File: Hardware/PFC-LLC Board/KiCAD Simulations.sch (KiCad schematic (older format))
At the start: 31 parts, among them J1 Conn_01x02_Female, P1 Conn_WallPlug_Earth, Q1 C2M0160120D, U1 UCC28180DR

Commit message: Start of PCB
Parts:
- Q1: footprint Package_TO_SOT_THT:TO-247-3_Vertical -> Package_TO_SOT_THT:TO-220-3_Vertical
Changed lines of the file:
@@
 F 0 "Q1" H 8854 2596 50  0000 L CNN
 F 1 "C2M0160120D" H 8854 2505 50  0000 L CNN
-F 2 "Package_TO_SOT_THT:TO-247-3_Vertical" H 8650 2550 50  0001 C CIN
+F 2 "Package_TO_SOT_THT:TO-220-3_Vertical" H 8650 2550 50  0001 C CIN
 F 3 "https://www.wolfspeed.com/media/downloads/169/C2M0160120D.pdf" H 8650 2550 50  0001 L CNN
 	1    8650 2550

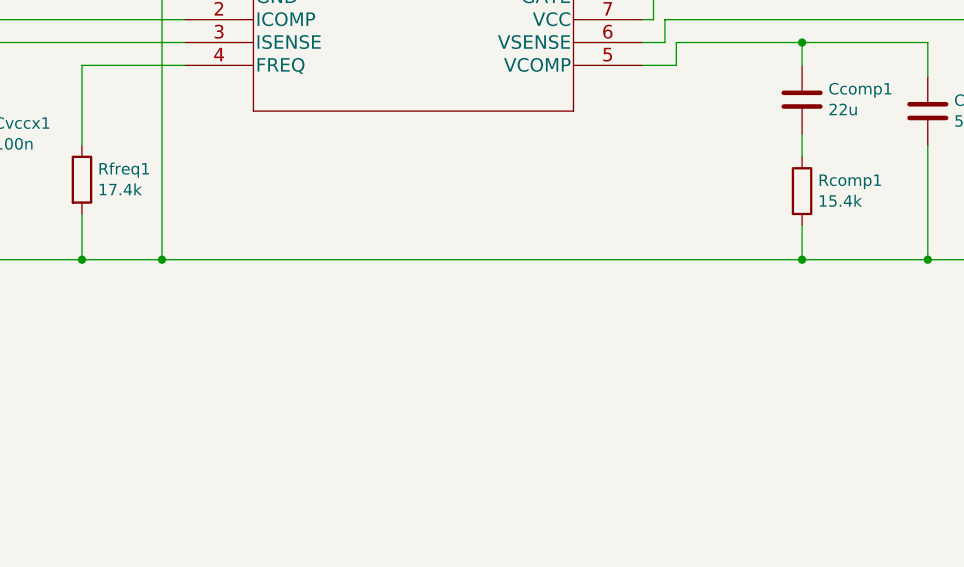
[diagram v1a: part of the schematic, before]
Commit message: Schematic/PCB updates
Minor updates to schematic and some place of PCB components as been done
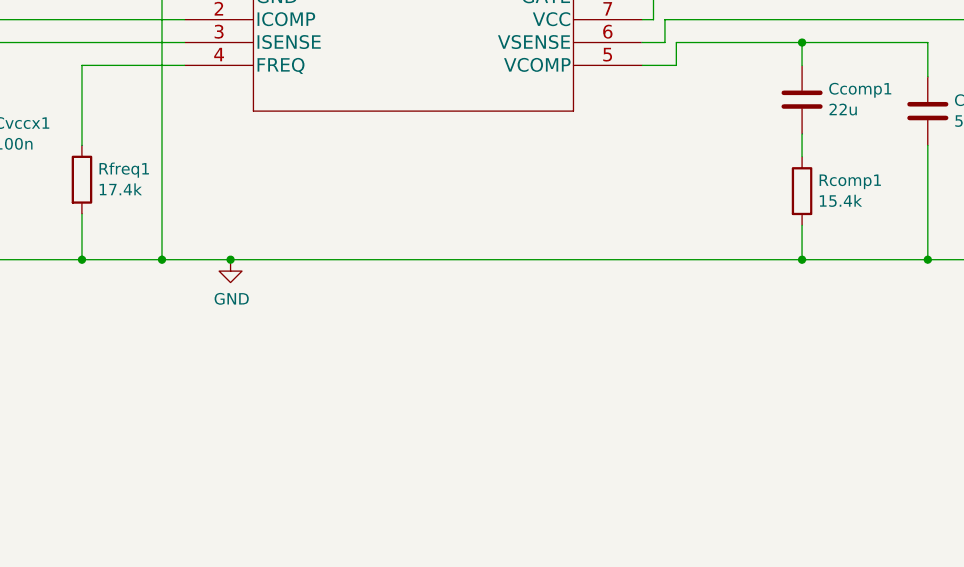
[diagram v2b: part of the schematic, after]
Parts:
- Q1: footprint Package_TO_SOT_THT:TO-220-3_Vertical -> Package_TO_SOT_THT:TO-247-3_Vertical
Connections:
- net labels added: GND
- wire segments 112 -> 113
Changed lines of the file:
@@
 F 0 "Q1" H 8854 2596 50  0000 L CNN
 F 1 "C2M0160120D" H 8854 2505 50  0000 L CNN
-F 2 "Package_TO_SOT_THT:TO-220-3_Vertical" H 8650 2550 50  0001 C CIN
+F 2 "Package_TO_SOT_THT:TO-247-3_Vertical" H 8650 2550 50  0001 C CIN
 F 3 "https://www.wolfspeed.com/media/downloads/169/C2M0160120D.pdf" H 8650 2550 50  0001 L CNN
 	1    8650 2550
@@
 Connection ~ 4950 5000
 Wire Wire Line
-	4950 5000 7750 5000
+	4950 5000 5250 5000
 $Comp
 L Connector:Conn_01x02_Female J1
@@
 F1 "LLC.sch" 50
 $EndSheet
+$Comp
+L power:GND #PWR0107
+U 1 1 6039E9A0
+P 5250 5000
+F 0 "#PWR0107" H 5250 4750 50  0001 C CNN
+F 1 "GND" H 5255 4827 50  0000 C CNN
+F 2 "" H 5250 5000 50  0001 C CNN
+F 3 "" H 5250 5000 50  0001 C CNN
+	1    5250 5000
+	1    0    0    -1
+$EndComp
+Connection ~ 5250 5000
+Wire Wire Line
+	5250 5000 7750 5000
 $EndSCHEMATC

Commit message: All footprints except PFC output caps
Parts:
- removed P1: Conn_WallPlug_Earth, symbol Connector:Conn_WallPlug_Earth
- added J1, J3: 1792229, Connector2x1:PHOENIX_1792229, symbol Connector2x1:1792229
- added Rntc1: 1, Resistor_THT:R_Box_L13.0mm_W4.0mm_P9.00mm, symbol Device:R
- L1: footprint (none) -> PFC_L1:IND_FIT106-2
- renumbered J1 to J2
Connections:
- wire segments 113 -> 120
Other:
- moved on the sheet: Ccomp1, Ccomp2, Cicomp1, Cin1, Cisense1, Cout1, Coutx1, Cvcc1, Cvccx1, Cvsense1, Dboost1, Disense1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

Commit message: All component footprints found and ready for PCB layout
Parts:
- removed Dboost1, Dstart1: 1N5406, Diode_THT:D_DO-201AD_P15.24mm_Horizontal, symbol Diode:1N5406
- added Dboost1: UF5406, Diode_THT:D_DO-201AD_P15.24mm_Horizontal, symbol Diode:UF5406
- added Dstart1: C3D10060A, Package_TO_SOT_THT:TO-220-2_Vertical, symbol Diode:C3D10060A
- Cout1: footprint (none) -> Capacitor_SMD:C_1206_3216Metric_Pad1.33x1.80mm_HandSolder
- Coutx1: footprint (none) -> Capacitor_THT:CP_Axial_L34.5mm_D20.0mm_P41.00mm_Horizontal
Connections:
- net at Cout1.1, Coutx1.1, J3.1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: now also Dboost1.1 (K), Dstart1.1 (K)
- net at L1.2, Q1.2 (D): now also Dboost1.2 (A)
- net at Cin1.1, L1.1, Uac1.3: now also Dstart1.2 (A)
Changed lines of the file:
@@
 F 0 "Cout1" H 9615 2146 50  0000 L CNN
 F 1 "18.113m" H 9615 2055 50  0000 L CNN
-F 2 "" H 9538 1950 50  0001 C CNN
+F 2 "Capacitor_SMD:C_1206_3216Metric_Pad1.33x1.80mm_HandSolder" H 9538 1950 50  0001 C CNN
 F 3 "~" H 9500 2100 50  0001 C CNN
 	1    9500 2100
@@
 F 0 "Coutx1" H 10265 2146 50  0000 L CNN
 F 1 "100n" H 10265 2055 50  0000 L CNN
-F 2 "" H 10188 1950 50  0001 C CNN
+F 2 "Capacitor_THT:CP_Axial_L34.5mm_D20.0mm_P41.00mm_Horizontal" H 10188 1950 50  0001 C CNN
 F 3 "~" H 10150 2100 50  0001 C CNN
 	1    10150 2100
@@
 	9500 2250 9500 2850
 Connection ~ 9500 2850
-$Comp
-L Diode:1N5406 Dboost1
-U 1 1 6011B734
-P 8350 1400
-F 0 "Dboost1" H 8350 1183 50  0000 C CNN
-F 1 "1N5406" H 8350 1274 50  0000 C CNN
-F 2 "Diode_THT:D_DO-201AD_P15.24mm_Horizontal" H 8350 1225 50  0001 C CNN
-F 3 "http://www.vishay.com/docs/88516/1n5400.pdf" H 8350 1400 50  0001 C CNN
-	1    8350 1400
-	-1   0    0    1
-$EndComp
 Wire Wire Line
 	8200 1400 8100 1400
@@
 Wire Wire Line
 	6650 1750 6800 1750
-$Comp
-L Diode:1N5406 Dstart1
-U 1 1 6013E3AC
-P 7150 950
-F 0 "Dstart1" H 7150 733 50  0000 C CNN
-F 1 "1N5406" H 7150 824 50  0000 C CNN
-F 2 "Diode_THT:D_DO-201AD_P15.24mm_Horizontal" H 7150 775 50  0001 C CNN
-F 3 "http://www.vishay.com/docs/88516/1n5400.pdf" H 7150 950 50  0001 C CNN
-	1    7150 950
-	-1   0    0    1
-$EndComp
 Wire Wire Line
 	7300 950  8650 950
@@
 	10550 2850 10150 2850
 Connection ~ 10150 2850
+$Comp
+L Diode:C3D10060A Dstart1
+U 1 1 60406B85
+P 7150 950
+F 0 "Dstart1" H 7150 733 50  0000 C CNN
+F 1 "C3D10060A" H 7150 824 50  0000 C CNN
+F 2 "Package_TO_SOT_THT:TO-220-2_Vertical" H 7150 775 50  0001 C CNN
+F 3 "https://www.wolfspeed.com/media/downloads/842/C3D10060A.pdf" H 7150 950 50  0001 C CNN
+	1    7150 950
+	-1   0    0    1
+$EndComp
+$Comp
+L Diode:UF5406 Dboost1
+U 1 1 60412A9A
+P 8350 1400
+F 0 "Dboost1" H 8350 1183 50  0000 C CNN
+F 1 "UF5406" H 8350 1274 50  0000 C CNN
+F 2 "Diode_THT:D_DO-201AD_P15.24mm_Horizontal" H 8350 1225 50  0001 C CNN
+F 3 "http://www.vishay.com/docs/88756/uf5400.pdf" H 8350 1400 50  0001 C CNN
+	1    8350 1400
+	-1   0    0    1
+$EndComp
 $EndSCHEMATC

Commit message: PCB with flooding (expect GND)
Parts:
- added TPgate1, TPisense1, TPvsense1: TestPoint, TestPoint:TestPoint_Pad_D1.0mm, symbol Connector:TestPoint
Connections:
- net at Cisense1.1, Disense1.1 (K), Risense1.1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: now also TPisense1.1
- net at Cvsense1.1, Rfbb1.1, Rfbt3.2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: now also TPvsense1.1
- net at Rgate3.2, U1.8 (GATE): now also TPgate1.1
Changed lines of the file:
@@
 	6500 3700 6400 3700
 Wire Wire Line
-	6500 3600 8200 3600
+	6500 3600 7800 3600
 Wire Wire Line
 	6550 3700 6550 3800
@@
 	1450 3600 4400 3600
 Wire Wire Line
-	2450 3700 4400 3700
+	2450 3700 3850 3700
 Wire Wire Line
 	3950 3800 4400 3800
@@
 	3950 4650 4300 4650
 Wire Wire Line
-	6400 3500 6650 3500
+	6400 3500 6500 3500
 Wire Wire Line
 	6400 3800 6550 3800
@@
 	-1   0    0    1
 $EndComp
+$Comp
+L Connector:TestPoint TPgate1
+U 1 1 60449B0C
+P 6500 3500
+F 0 "TPgate1" H 6558 3618 50  0000 L CNN
+F 1 "TestPoint" H 6558 3527 50  0000 L CNN
+F 2 "TestPoint:TestPoint_Pad_D1.0mm" H 6700 3500 50  0001 C CNN
+F 3 "~" H 6700 3500 50  0001 C CNN
+	1    6500 3500
+	1    0    0    -1
+$EndComp
+Connection ~ 6500 3500
+Wire Wire Line
+	6500 3500 6650 3500
+$Comp
+L Connector:TestPoint TPvsense1
+U 1 1 6044C5BE
+P 7800 3600
+F 0 "TPvsense1" H 7858 3718 50  0000 L CNN
+F 1 "TestPoint" H 7858 3627 50  0000 L CNN
+F 2 "TestPoint:TestPoint_Pad_D1.0mm" H 8000 3600 50  0001 C CNN
+F 3 "~" H 8000 3600 50  0001 C CNN
+	1    7800 3600
+	1    0    0    -1
+$EndComp
+Connection ~ 7800 3600
+Wire Wire Line
+	7800 3600 8200 3600
+$Comp
+L Connector:TestPoint TPisense1
+U 1 1 6044D3B8
+P 3850 3700
+F 0 "TPisense1" H 3908 3818 50  0000 L CNN
+F 1 "TestPoint" H 3908 3727 50  0000 L CNN
+F 2 "TestPoint:TestPoint_Pad_D1.0mm" H 4050 3700 50  0001 C CNN
+F 3 "~" H 4050 3700 50  0001 C CNN
+	1    3850 3700
+	1    0    0    -1
+$EndComp
+Connection ~ 3850 3700
+Wire Wire Line
+	3850 3700 4400 3700
 $EndSCHEMATC

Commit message: Gerber files generated
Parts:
- Cin1: value 221.893n -> 10n
- Cout1: value 18.113m -> 13.585m
- L1: value 148.268u -> 197.691u
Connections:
- net GND: now also Cout1.2, Coutx1.2, J3.2, Q1.3 (S), Rgate2.2, Rsense1.2
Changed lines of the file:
@@
 P 9500 2100
 F 0 "Cout1" H 9615 2146 50  0000 L CNN
-F 1 "18.113m" H 9615 2055 50  0000 L CNN
+F 1 "13.585m" H 9615 2055 50  0000 L CNN
 F 2 "Capacitor_SMD:C_1206_3216Metric_Pad1.33x1.80mm_HandSolder" H 9538 1950 50  0001 C CNN
 F 3 "~" H 9500 2100 50  0001 C CNN
@@
 	10150 2250 10150 2850
 Wire Wire Line
-	10150 2850 9500 2850
+	10150 2850 9550 2850
 Wire Wire Line
 	9500 2250 9500 2850
@@
 P 6300 1400
 F 0 "L1" V 6490 1400 50  0000 C CNN
-F 1 "148.268u" V 6399 1400 50  0000 C CNN
+F 1 "197.691u" V 6399 1400 50  0000 C CNN
 F 2 "PFC_L1:IND_FIT106-2" H 6300 1400 50  0001 C CNN
 F 3 "~" H 6300 1400 50  0001 C CNN
@@
 P 4600 2050
 F 0 "Cin1" H 4715 2096 50  0000 L CNN
-F 1 "221.893n" H 4715 2005 50  0000 L CNN
+F 1 "10n" H 4715 2005 50  0000 L CNN
 F 2 "Capacitor_SMD:C_0805_2012Metric_Pad1.18x1.45mm_HandSolder" H 4638 1900 50  0001 C CNN
 F 3 "~" H 4600 2050 50  0001 C CNN
@@
 Wire Wire Line
 	3850 3700 4400 3700
+Wire Wire Line
+	9550 2850 9550 4650
+Wire Wire Line
+	9550 4650 8800 4650
+Connection ~ 9550 2850
+Wire Wire Line
+	9550 2850 9500 2850
+Connection ~ 8800 4650
 $EndSCHEMATC

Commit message: Added Test points
Added Test points
Changed Capacitor Values around
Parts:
- removed Cin1: 10n, Capacitor_SMD:C_0805_2012Metric_Pad1.18x1.45mm_HandSolder, symbol Device:C
- removed Cout1: 13.585m, Capacitor_SMD:C_1206_3216Metric_Pad1.33x1.80mm_HandSolder, symbol Device:C
- added Cin, Coutx2: 100n, Capacitor_THT:CP_Axial_L34.5mm_D20.0mm_P41.00mm_Horizontal, symbol KiCAD-Simulations-rescue:C-Device
- added TPDstart: TestPoint Dstart, TestPoint:TestPoint_Pad_D1.0mm, symbol KiCAD-Simulations-rescue:TestPoint-Connector
- added TPDstart2: TestPoint Dstart2, TestPoint:TestPoint_Pad_D1.0mm, symbol KiCAD-Simulations-rescue:TestPoint-Connector
- added TPQ1: TestPoint Q1, TestPoint:TestPoint_Pad_D1.0mm, symbol KiCAD-Simulations-rescue:TestPoint-Connector
- added TPgnd1, TPgnd2, TPgnd3, TPgnd4: TestPoint GND, TestPoint:TestPoint_Pad_D1.0mm, symbol KiCAD-Simulations-rescue:TestPoint-Connector
- added TPgnd5: TestPoint GND Q1, TestPoint:TestPoint_Pad_D1.0mm, symbol KiCAD-Simulations-rescue:TestPoint-Connector
- Ccomp1, Ccomp2, Cicomp1, Cisense1, Coutx1, Cvccx1, Cvsense1: symbol Device:C -> KiCAD-Simulations-rescue:C-Device
- Cvcc1: symbol Device:CP -> KiCAD-Simulations-rescue:CP-Device
- Dboost1: symbol Diode:UF5406 -> KiCAD-Simulations-rescue:UF5406-Diode
- Disense1: symbol Diode:1N4148 -> KiCAD-Simulations-rescue:1N4148-Diode
- Dstart1: symbol Diode:C3D10060A -> KiCAD-Simulations-rescue:C3D10060A-Diode
- Dturnoff1: symbol Diode:B240 -> KiCAD-Simulations-rescue:B240-Diode
- J1, J3: symbol Connector2x1:1792229 -> KiCAD-Simulations-rescue:1792229-Connector2x1
- J2: symbol Connector:Conn_01x02_Female -> KiCAD-Simulations-rescue:Conn_01x02_Female-Connector
- L1: symbol Device:L -> KiCAD-Simulations-rescue:L-Device
- Q1: symbol Transistor_FET:C2M0160120D -> KiCAD-Simulations-rescue:C2M0160120D-Transistor_FET
- Rcomp1, Rfbb1, Rfbt1, Rfbt2, Rfbt3, Rfreq1, Rgate2, Rgate3, Risense1, Rntc1, Rsense1: symbol Device:R -> KiCAD-Simulations-rescue:R-Device
- Rgate1: value 1.07 -> 1.00; symbol Device:R -> KiCAD-Simulations-rescue:R-Device
- TPgate1: value TestPoint -> TestPoint Gate Pin; symbol Connector:TestPoint -> KiCAD-Simulations-rescue:TestPoint-Connector
- TPisense1, TPvsense1: symbol Connector:TestPoint -> KiCAD-Simulations-rescue:TestPoint-Connector
- U1: symbol PFC_IC:UCC28180DR -> KiCAD-Simulations-rescue:UCC28180DR-PFC_IC
- Uac1: symbol PFC_Dac:GBJ2510-F -> KiCAD-Simulations-rescue:GBJ2510-F-PFC_Dac
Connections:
- net GND: now also Coutx2.2, TPgnd1.1, TPgnd2.1, TPgnd3.1, TPgnd4.1, TPgnd5.1
- net at Risense1.2, Rsense1.1, Uac1.2: now also Cin.2
- net at Coutx1.1, Dboost1.1 (K), Dstart1.1 (K)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: now also Coutx2.1, TPDstart2.1
- net at Dturnoff1.1 (K), Rgate3.1: no longer Rgate1.1
- net at Rgate3.2, TPgate1.1, U1.8 (GATE): now also Rgate1.1
- net at Dturnoff1.2 (A), Q1.1 (G), Rgate1.2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: now also TPQ1.1
- net at Dstart1.2 (A), L1.1, Uac1.3: now also Cin.1, TPDstart.1
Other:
- moved on the sheet: Dturnoff1, Rgate1, Rgate2, Rgate3

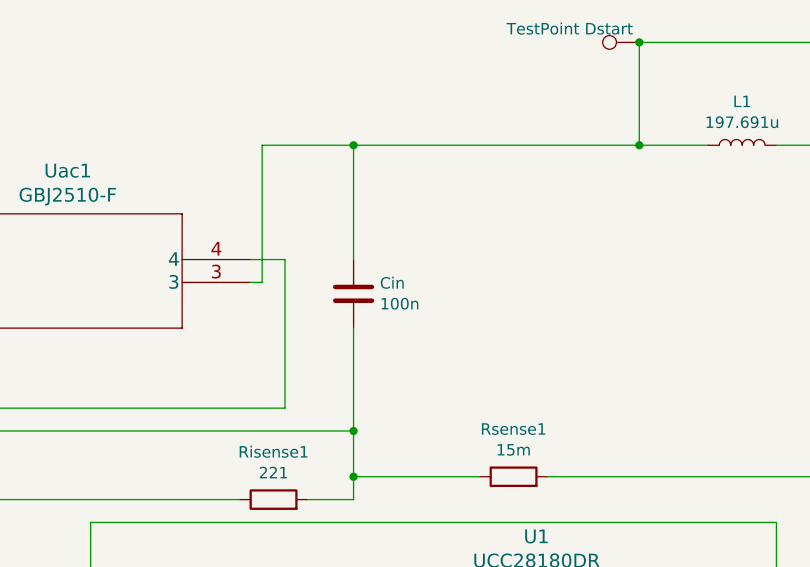
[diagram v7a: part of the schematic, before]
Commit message: PFC footprints updated
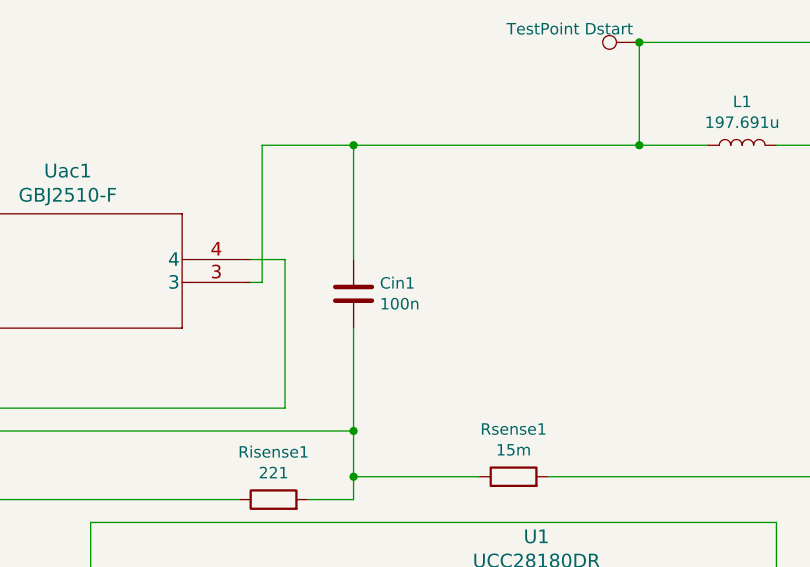
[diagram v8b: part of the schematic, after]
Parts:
- Ccomp1, Cicomp1: footprint Capacitor_SMD:C_0805_2012Metric_Pad1.18x1.45mm_HandSolder -> Capacitor_SMD:C_1206_3216Metric_Pad1.33x1.80mm_HandSolder
- Ccomp2, Cvccx1: footprint Capacitor_SMD:C_0402_1005Metric_Pad0.74x0.62mm_HandSolder -> Capacitor_SMD:C_1206_3216Metric_Pad1.33x1.80mm_HandSolder
- Cisense1, Cvsense1: footprint Capacitor_SMD:C_0201_0603Metric_Pad0.64x0.40mm_HandSolder -> Capacitor_SMD:C_1206_3216Metric_Pad1.33x1.80mm_HandSolder
- Rcomp1, Rfbb1, Rgate2: footprint Resistor_SMD:R_0201_0603Metric_Pad0.64x0.40mm_HandSolder -> Resistor_SMD:R_2512_6332Metric_Pad1.40x3.35mm_HandSolder
- Rfreq1, Rgate1, Rgate3, Risense1: footprint Resistor_SMD:R_0402_1005Metric_Pad0.72x0.64mm_HandSolder -> Resistor_SMD:R_2512_6332Metric_Pad1.40x3.35mm_HandSolder
- Rsense1: footprint Resistor_SMD:R_1206_3216Metric_Pad1.30x1.75mm_HandSolder -> Resistor_SMD:R_2512_6332Metric_Pad1.40x3.35mm_HandSolder
- renumbered Cin to Cin1, TPDstart to TPDstart1
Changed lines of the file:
@@
 F 0 "Risense1" V 4457 2950 50  0000 C CNN
 F 1 "221" V 4366 2950 50  0000 C CNN
-F 2 "Resistor_SMD:R_0402_1005Metric_Pad0.72x0.64mm_HandSolder" V 4180 2950 50  0001 C CNN
+F 2 "Resistor_SMD:R_2512_6332Metric_Pad1.40x3.35mm_HandSolder" V 4180 2950 50  0001 C CNN
 F 3 "~" H 4250 2950 50  0001 C CNN
 	1    4250 2950
@@
 F 0 "Cisense1" H 2565 4146 50  0000 L CNN
 F 1 "1n" H 2565 4055 50  0000 L CNN
-F 2 "Capacitor_SMD:C_0201_0603Metric_Pad0.64x0.40mm_HandSolder" H 2488 3950 50  0001 C CNN
+F 2 "Capacitor_SMD:C_1206_3216Metric_Pad1.33x1.80mm_HandSolder" H 2488 3950 50  0001 C CNN
 F 3 "~" H 2450 4100 50  0001 C CNN
 	1    2450 4100
@@
 F 0 "Rfreq1" H 4020 4346 50  0000 L CNN
 F 1 "17.4k" H 4020 4255 50  0000 L CNN
-F 2 "Resistor_SMD:R_0402_1005Metric_Pad0.72x0.64mm_HandSolder" V 3880 4300 50  0001 C CNN
+F 2 "Resistor_SMD:R_2512_6332Metric_Pad1.40x3.35mm_HandSolder" V 3880 4300 50  0001 C CNN
 F 3 "~" H 3950 4300 50  0001 C CNN
 	1    3950 4300
@@
 F 0 "Ccomp1" H 7215 3996 50  0000 L CNN
 F 1 "22u" H 7215 3905 50  0000 L CNN
-F 2 "Capacitor_SMD:C_0805_2012Metric_Pad1.18x1.45mm_HandSolder" H 7138 3800 50  0001 C CNN
+F 2 "Capacitor_SMD:C_1206_3216Metric_Pad1.33x1.80mm_HandSolder" H 7138 3800 50  0001 C CNN
 F 3 "~" H 7100 3950 50  0001 C CNN
 	1    7100 3950
@@
 F 0 "Rcomp1" H 7170 4396 50  0000 L CNN
 F 1 "15.4k" H 7170 4305 50  0000 L CNN
-F 2 "Resistor_SMD:R_0201_0603Metric_Pad0.64x0.40mm_HandSolder" V 7030 4350 50  0001 C CNN
+F 2 "Resistor_SMD:R_2512_6332Metric_Pad1.40x3.35mm_HandSolder" V 7030 4350 50  0001 C CNN
 F 3 "~" H 7100 4350 50  0001 C CNN
 	1    7100 4350
@@
 F 0 "Ccomp2" H 7765 4046 50  0000 L CNN
 F 1 "560n" H 7765 3955 50  0000 L CNN
-F 2 "Capacitor_SMD:C_0402_1005Metric_Pad0.74x0.62mm_HandSolder" H 7688 3850 50  0001 C CNN
+F 2 "Capacitor_SMD:C_1206_3216Metric_Pad1.33x1.80mm_HandSolder" H 7688 3850 50  0001 C CNN
 F 3 "~" H 7650 4000 50  0001 C CNN
 	1    7650 4000
@@
 F 0 "Cvsense1" H 8315 4046 50  0000 L CNN
 F 1 "4.7n" H 8315 3955 50  0000 L CNN
-F 2 "Capacitor_SMD:C_0201_0603Metric_Pad0.64x0.40mm_HandSolder" H 8238 3850 50  0001 C CNN
+F 2 "Capacitor_SMD:C_1206_3216Metric_Pad1.33x1.80mm_HandSolder" H 8238 3850 50  0001 C CNN
 F 3 "~" H 8200 4000 50  0001 C CNN
 	1    8200 4000
@@
 F 0 "Rfbb1" H 8870 4046 50  0000 L CNN
 F 1 "12.1k" H 8870 3955 50  0000 L CNN
-F 2 "Resistor_SMD:R_0201_0603Metric_Pad0.64x0.40mm_HandSolder" V 8730 4000 50  0001 C CNN
+F 2 "Resistor_SMD:R_2512_6332Metric_Pad1.40x3.35mm_HandSolder" V 8730 4000 50  0001 C CNN
 F 3 "~" H 8800 4000 50  0001 C CNN
 	1    8800 4000
@@
 F 0 "Rsense1" V 5507 2850 50  0000 C CNN
 F 1 "15m" V 5416 2850 50  0000 C CNN
-F 2 "Resistor_SMD:R_1206_3216Metric_Pad1.30x1.75mm_HandSolder" V 5230 2850 50  0001 C CNN
+F 2 "Resistor_SMD:R_2512_6332Metric_Pad1.40x3.35mm_HandSolder" V 5230 2850 50  0001 C CNN
 F 3 "~" H 5300 2850 50  0001 C CNN
 	1    5300 2850
@@
 F 0 "Rgate2" H 7570 2646 50  0000 L CNN
 F 1 "10k" H 7570 2555 50  0000 L CNN
-F 2 "Resistor_SMD:R_0201_0603Metric_Pad0.64x0.40mm_HandSolder" V 7430 2600 50  0001 C CNN
+F 2 "Resistor_SMD:R_2512_6332Metric_Pad1.40x3.35mm_HandSolder" V 7430 2600 50  0001 C CNN
 F 3 "~" H 7500 2600 50  0001 C CNN
 	1    7500 2600
@@
 F 0 "Rgate1" V 7457 2350 50  0000 C CNN
 F 1 "1.00" V 7366 2350 50  0000 C CNN
-F 2 "Resistor_SMD:R_0402_1005Metric_Pad0.72x0.64mm_HandSolder" V 7180 2350 50  0001 C CNN
+F 2 "Resistor_SMD:R_2512_6332Metric_Pad1.40x3.35mm_HandSolder" V 7180 2350 50  0001 C CNN
 F 3 "~" H 7250 2350 50  0001 C CNN
 	1    7250 2350
@@
 F 0 "Cvccx1" H 3565 4146 50  0000 L CNN
 F 1 "100n" H 3565 4055 50  0000 L CNN
-F 2 "Capacitor_SMD:C_0402_1005Metric_Pad0.74x0.62mm_HandSolder" H 3488 3950 50  0001 C CNN
+F 2 "Capacitor_SMD:C_1206_3216Metric_Pad1.33x1.80mm_HandSolder" H 3488 3950 50  0001 C CNN
 F 3 "~" H 3450 4100 50  0001 C CNN
 	1    3450 4100
@@
 F 0 "Cicomp1" H 1565 4146 50  0000 L CNN
 F 1 "3.3n" H 1565 4055 50  0000 L CNN
-F 2 "Capacitor_SMD:C_0805_2012Metric_Pad1.18x1.45mm_HandSolder" H 1488 3950 50  0001 C CNN
+F 2 "Capacitor_SMD:C_1206_3216Metric_Pad1.33x1.80mm_HandSolder" H 1488 3950 50  0001 C CNN
 F 3 "~" H 1450 4100 50  0001 C CNN
 	1    1450 4100
@@
 F 0 "Rgate3" H 6770 2196 50  0000 L CNN
 F 1 "3.92" H 6770 2105 50  0000 L CNN
-F 2 "Resistor_SMD:R_0402_1005Metric_Pad0.72x0.64mm_HandSolder" V 6630 2150 50  0001 C CNN
+F 2 "Resistor_SMD:R_2512_6332Metric_Pad1.40x3.35mm_HandSolder" V 6630 2150 50  0001 C CNN
 F 3 "~" H 6700 2150 50  0001 C CNN
 	1    6700 2150
@@
 $EndComp
 $Comp
-L KiCAD-Simulations-rescue:C-Device Cin
+L KiCAD-Simulations-rescue:C-Device Cin1
 U 1 1 604BB2B6
 P 4600 2050
-F 0 "Cin" H 4715 2096 50  0000 L CNN
+F 0 "Cin1" H 4715 2096 50  0000 L CNN
 F 1 "100n" H 4715 2005 50  0000 L CNN
 F 2 "Capacitor_THT:CP_Axial_L34.5mm_D20.0mm_P41.00mm_Horizontal" H 4638 1900 50  0001 C CNN
@@
 $EndComp
 $Comp
-L KiCAD-Simulations-rescue:TestPoint-Connector TPDstart
+L KiCAD-Simulations-rescue:TestPoint-Connector TPDstart1
 U 1 1 604E97D9
 P 5850 950
-F 0 "TPDstart" V 5908 1068 50  0001 L BNN
+F 0 "TPDstart1" V 5908 1068 50  0001 L BNN
 F 1 "TestPoint Dstart" V 5908 977 50  0000 L CNN
 F 2 "TestPoint:TestPoint_Pad_D1.0mm" H 6050 950 50  0001 C CNN
